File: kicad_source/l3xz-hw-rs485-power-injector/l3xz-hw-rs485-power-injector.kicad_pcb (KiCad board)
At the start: 2 copper layers, 38 x 55 mm, 27 parts, among them J1 PowerPole, J2 Conn_01x02, J3 Conn_01x03, J4 SM04B-GHS-TB, J5 EH_S4B-EH, J6 EH_S4B-EH, J7 Conn_01x04, U1 L78L05_SOT89, U2 SN75176AD

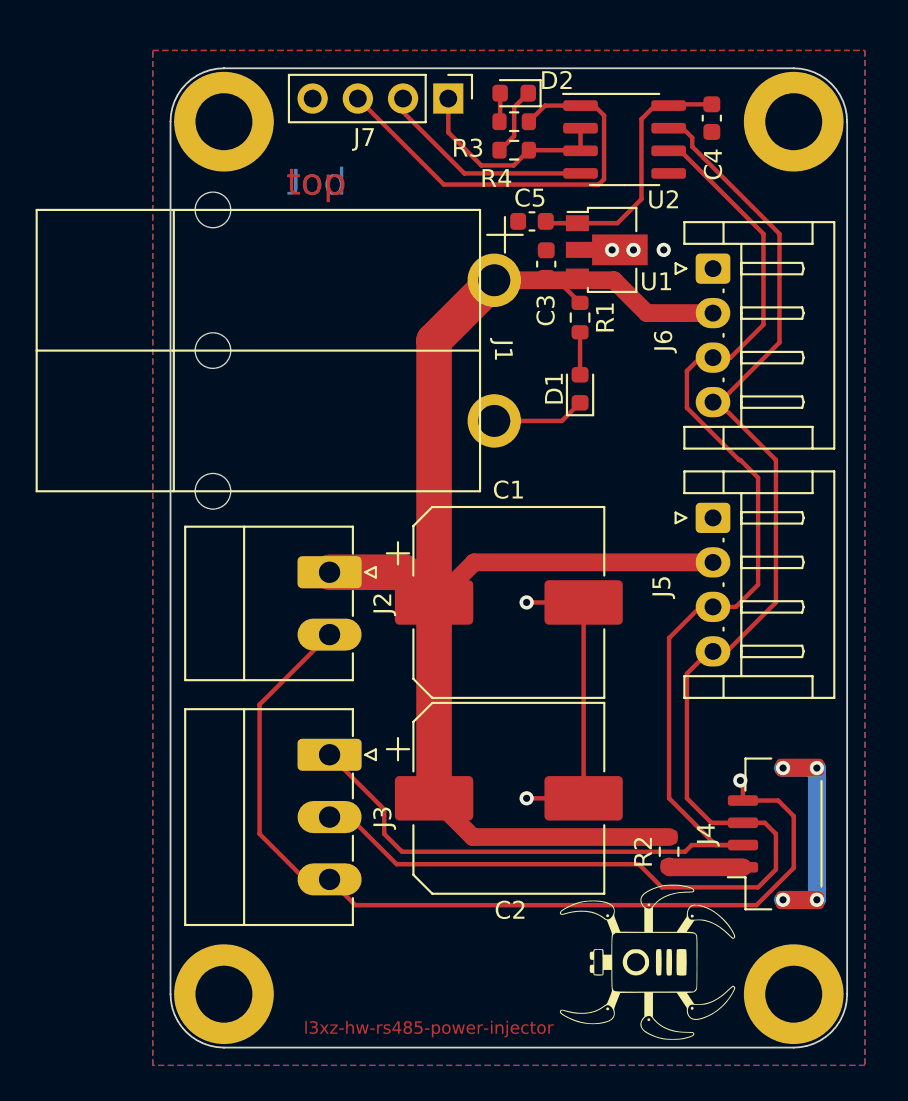
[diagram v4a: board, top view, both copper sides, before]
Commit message: added some labels
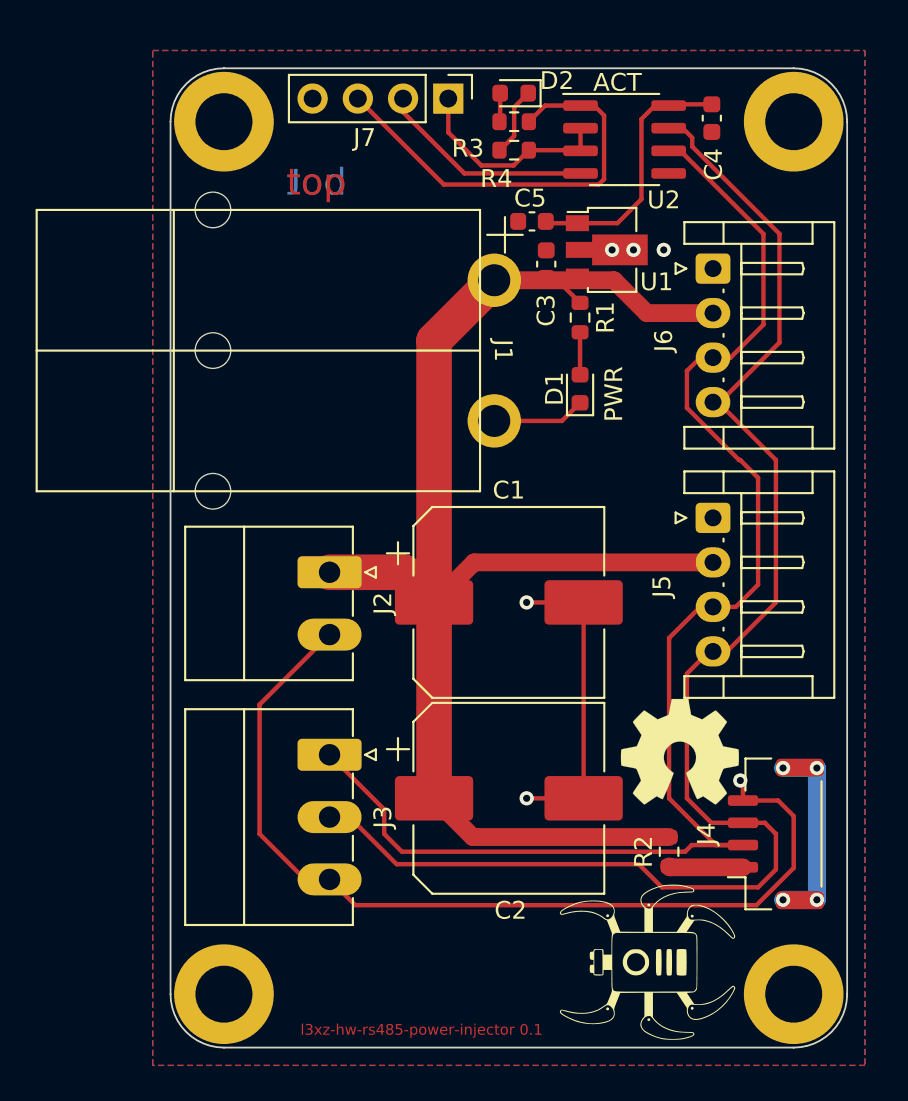
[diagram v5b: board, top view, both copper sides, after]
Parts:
- added L4: Label, Symbol:OSHW-Symbol_6.7x6mm_SilkScreen, F.Cu at (154.6, 91.4)
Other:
- board text added: "+"
- board text added: "+BATT"
- board text added: "ACT"
- board text added: "GND"
- board text added: "PWR"
- board text added: "RS485-A"
- board text added: "RS485-B"
- board text added: "RS485-RX"
- board text added: "RS485-TX"
- board text added: "RS485-TXEN"
- board text added: "https://github.com/107-systems/ l3xz-hw-rs485-power-injector"
- board text added: "l3xz-hw-rs485-power-injector 0.1"
- board text added: "max. input voltage depends on used dynamixel servo"
- board text removed: "l3xz-hw-rs485-power-injector"

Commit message: added some gnd vias
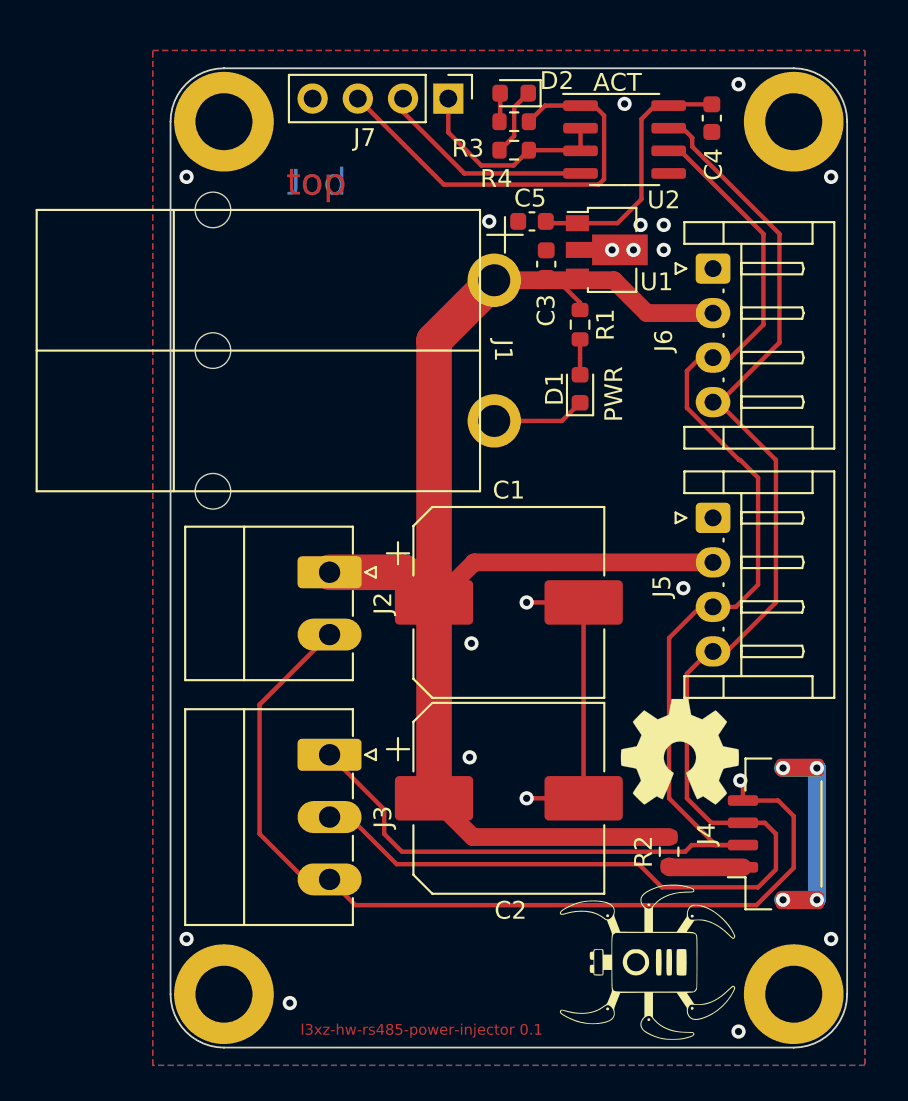
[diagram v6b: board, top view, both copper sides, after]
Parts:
- J2: value Conn_01x02 -> DNI
- J3: value Conn_01x03 -> DNI
- J7: value Conn_01x04 -> DNI
- moved R1 0.40 mm to (149.0, 67.4)
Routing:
- net GND: vias 6 -> 20
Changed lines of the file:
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@@
     (property "Sheetfile" "l3xz-hw-rs485-power-injector.kicad_sch")
     (property "Sheetname" "")
-    (attr board_only exclude_from_pos_files)
+    (property "exclude_from_bom" "")
+    (attr board_only exclude_from_pos_files exclude_from_bom)
     (fp_text reference "L3" (at 0 0 90) (layer "F.SilkS") hide
       (effects (font (size 1.524 1.524) (thickness 0.3)))
@@
   )
   (footprint "Resistor_SMD:R_0603_1608Metric" (layer "F.Cu")
-    (at 149 67 -90)
+    (at 149 67.4 -90)
     (descr "Resistor SMD 0603 (1608 Metric), square (rectangular) end terminal, IPC_7351 nominal, (Body size source: IPC-SM-782 page 72, https://www.pcb-3d.com/wordpress/wp-content/uploads/ipc-sm-782a_amendment_1_and_2.pdf), generated with kicad-footprint-generator")
     (tags "resistor")
@@
       (effects (font (size 1 1) (thickness 0.15)))
     )
-    (fp_text value "Conn_01x03" (at 3.5 9.2 90) (layer "F.Fab")
+    (fp_text value "DNI" (at 3.5 9.2 90) (layer "F.Fab")
       (effects (font (size 1 1) (thickness 0.15)))
     )
@@
     (property "Sheetfile" "l3xz-hw-rs485-power-injector.kicad_sch")
     (property "Sheetname" "")
-    (attr through_hole)
+    (property "exclude_from_bom" "")
+    (attr through_hole exclude_from_bom)
     (fp_text reference "L1" (at 0 0) (layer "F.SilkS") hide
       (effects (font (size 1.524 1.524) (thickness 0.3)))
@@
     (property "Sheetfile" "l3xz-hw-rs485-power-injector.kicad_sch")
     (property "Sheetname" "")
-    (attr exclude_from_pos_files)
+    (property "exclude_from_bom" "")
+    (attr exclude_from_pos_files exclude_from_bom)
     (fp_text reference "L4" (at 0 0) (layer "F.SilkS") hide
       (effects (font (size 1 1) (thickness 0.15)))
@@
       (effects (font (size 1 1) (thickness 0.15)))
     )
-    (fp_text value "Conn_01x04" (at 0 9.95 90) (layer "F.Fab")
+    (fp_text value "DNI" (at 0 9.95 90) (layer "F.Fab")
       (effects (font (size 1 1) (thickness 0.15)))
     )
@@
       (effects (font (size 1 1) (thickness 0.15)))
     )
-    (fp_text value "Conn_01x02" (at 1.75 9.2 90) (layer "F.Fab")
+    (fp_text value "DNI" (at 1.75 9.2 90) (layer "F.Fab")
       (effects (font (size 1 1) (thickness 0.15)))
     )
@@
     (property "Sheetfile" "l3xz-hw-rs485-power-injector.kicad_sch")
     (property "Sheetname" "")
-    (attr board_only exclude_from_pos_files)
+    (property "exclude_from_bom" "")
+    (attr board_only exclude_from_pos_files exclude_from_bom)
     (fp_text reference "L2" (at 0 0 90) (layer "B.SilkS") hide
       (effects (font (size 1.524 1.524) (thickness 0.3)) (justify mirror))
@@
   (segment (start 142.975 96.175) (end 140.8 94) (width 1) (layer "F.Cu") (net 1))
   (segment (start 140.8 94) (end 140.8 83) (width 2) (layer "F.Cu") (net 1))
+  (segment (start 149 66.175) (end 149 66.575) (width 0.25) (layer "F.Cu") (net 1))
   (segment (start 139.105 81.305) (end 140.8 83) (width 2) (layer "F.Cu") (net 1))
   (segment (start 147.73 64.905) (end 144.1825 64.905) (width 0.25) (layer "F.Cu") (net 1))
@@
   (segment (start 158.15 94.125) (end 160.125 94.125) (width 0.25) (layer "F.Cu") (net 2))
   (segment (start 158.15 94.125) (end 158.15 93.15) (width 0.25) (layer "F.Cu") (net 2))
+  (via (at 142.8 91.7) (size 0.8) (drill 0.4) (layers "F.Cu" "B.Cu") (free) (net 2))
   (via (at 152 63.2) (size 0.8) (drill 0.4) (layers "F.Cu" "B.Cu") (net 2))
+  (via (at 143.9 61.6) (size 0.8) (drill 0.4) (layers "F.Cu" "B.Cu") (free) (net 2))
+  (via (at 157.9 107.1) (size 0.8) (drill 0.4) (layers "F.Cu" "B.Cu") (free) (net 2))
+  (via (at 154.8 82.2) (size 0.8) (drill 0.4) (layers "F.Cu" "B.Cu") (free) (net 2))
+  (via (at 126.9 59.1) (size 0.8) (drill 0.4) (layers "F.Cu" "B.Cu") (free) (net 2))
   (via (at 150.8 63.2) (size 0.8) (drill 0.4) (layers "F.Cu" "B.Cu") (net 2))
+  (via (at 163.1 101.9) (size 0.8) (drill 0.4) (layers "F.Cu" "B.Cu") (free) (net 2))
+  (via (at 142.9 85.3) (size 0.8) (drill 0.4) (layers "F.Cu" "B.Cu") (free) (net 2))
   (via (at 146 94) (size 0.8) (drill 0.4) (layers "F.Cu" "B.Cu") (net 2))
+  (via (at 153.7 61.8) (size 0.8) (drill 0.4) (layers "F.Cu" "B.Cu") (free) (net 2))
+  (via (at 151.5 55) (size 0.8) (drill 0.4) (layers "F.Cu" "B.Cu") (free) (net 2))
   (via (at 158 93) (size 0.8) (drill 0.4) (layers "F.Cu" "B.Cu") (net 2))
+  (via (at 157.9 53.9) (size 0.8) (drill 0.4) (layers "F.Cu" "B.Cu") (free) (net 2))
+  (via (at 132.7 105.5) (size 0.8) (drill 0.4) (layers "F.Cu" "B.Cu") (free) (net 2))
   (via (at 146 83) (size 0.8) (drill 0.4) (layers "F.Cu" "B.Cu") (net 2))
+  (via (at 163.1 59.1) (size 0.8) (drill 0.4) (layers "F.Cu" "B.Cu") (free) (net 2))
   (via (at 153.7 63.2) (size 0.8) (drill 0.4) (layers "F.Cu" "B.Cu") (free) (net 2))
+  (via (at 152.4 61.8) (size 0.8) (drill 0.4) (layers "F.Cu" "B.Cu") (free) (net 2))
+  (via (at 126.9 101.9) (size 0.8) (drill 0.4) (layers "F.Cu" "B.Cu") (free) (net 2))
   (segment (start 158.15 96.625) (end 155.275 96.625) (width 0.25) (layer "F.Cu") (net 3))
   (segment (start 156.4675 83.25) (end 157.75 83.25) (width 0.25) (layer "F.Cu") (net 3))
@@
   (segment (start 158.15 97.875) (end 154.05 97.875) (width 1) (layer "F.Cu") (net 5))
   (segment (start 154.05 97.875) (end 154 97.825) (width 1) (layer "F.Cu") (net 5))
-  (segment (start 149 70.2125) (end 149 67.825) (width 0.25) (layer "F.Cu") (net 6))
+  (segment (start 149 69.3) (end 149 68.225) (width 0.25) (layer "F.Cu") (net 6))
+  (segment (start 149 70.2125) (end 149 69.3) (width 0.25) (layer "F.Cu") (net 6))
   (segment (start 153.205 55.095) (end 152.45 55.85) (width 0.25) (layer "F.Cu") (net 11))
   (segment (start 147.175 61.7) (end 147.075 61.6) (width 0.25) (layer "F.Cu") (net 11))
